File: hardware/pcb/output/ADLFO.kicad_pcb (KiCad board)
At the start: 2 copper layers, 116.6 x 110.5 mm, 118 parts, among them J1 TRIG1, J10 TRIG4, J11 CV4, J12 OUT4, J13 EURORACK 2x5 keyed, J14 OLED SSD1306 128x64, J2 CV1, J3 OUT1, J4 TRIG2, J5 CV2, J6 OUT2, J7 TRIG3, J8 CV3, J9 OUT3, Q1 MMBT3904, Q2 MMBT3904, Q3 MMBT3904, Q4 MMBT3904, SW1 CH 1, SW2 CH 2, SW3 CH 3, SW4 CH 4, U1 Daisy Seed (socketed), U2 MCP4728-E/UN, U3 MCP6004-I/SL, U4 TL074CDR, U5 R-78E5.0-0.5

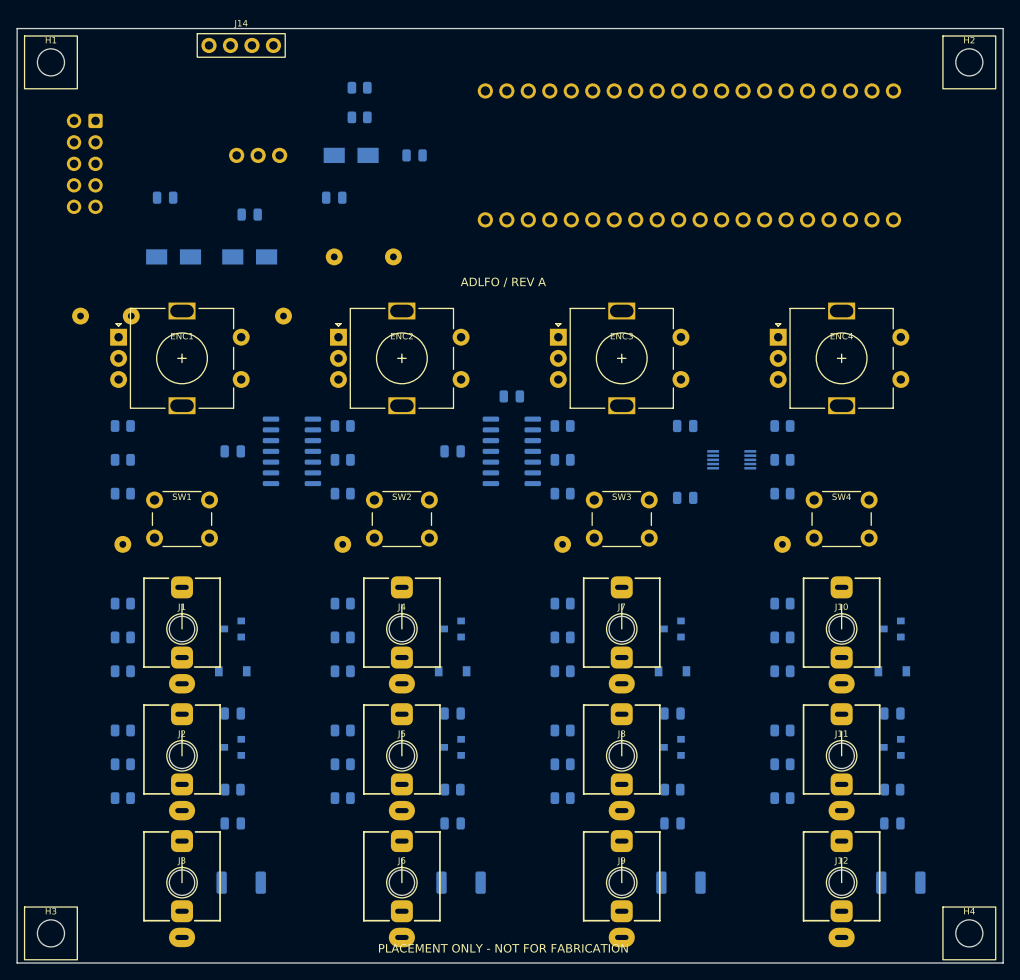
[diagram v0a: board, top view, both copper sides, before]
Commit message: Adapt PCB placement to 20 HP with Adafruit DAC module and Eurorack power provisions
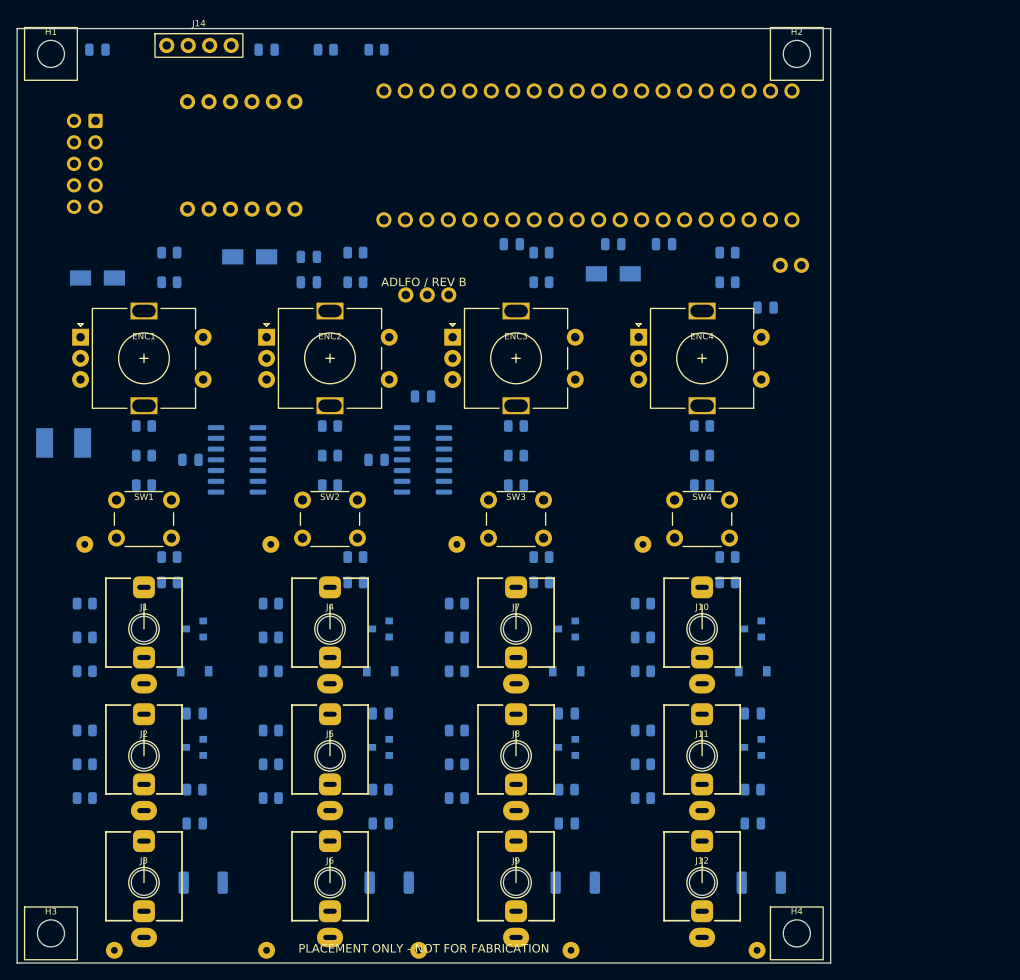
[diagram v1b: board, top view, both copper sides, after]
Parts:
- added C10: 47uF 10V low ESR candidate, ADLFO:radial_cap, B.Cu at (94.0, 37.0)
- added C11: 100nF, ADLFO:c0805, B.Cu at (79.0, 34.5)
- added C12: 100nF, ADLFO:c0805, B.Cu at (91.0, 42.0)
- added F1: PTC 0.5A hold candidate, ADLFO:ptc1812, B.Cu at (8.00, 58.0)
- added RP11: 10k DNP, ADLFO:r0805, B.Cu at (20.5, 35.5)
- added RP12: 10k DNP, ADLFO:r0805, B.Cu at (20.5, 39.0)
- added RP13: 10k DNP, ADLFO:r0805, B.Cu at (20.5, 71.5)
- added RP14: 10k DNP, ADLFO:r0805, B.Cu at (20.5, 74.5)
- added RP21: 10k DNP, ADLFO:r0805, B.Cu at (42.5, 35.5)
- added RP22: 10k DNP, ADLFO:r0805, B.Cu at (42.5, 39.0)
- added RP23: 10k DNP, ADLFO:r0805, B.Cu at (42.5, 71.5)
- added RP24: 10k DNP, ADLFO:r0805, B.Cu at (42.5, 74.5)
- added RP31: 10k DNP, ADLFO:r0805, B.Cu at (64.5, 35.5)
- added RP32: 10k DNP, ADLFO:r0805, B.Cu at (64.5, 39.0)
- added RP33: 10k DNP, ADLFO:r0805, B.Cu at (64.5, 71.5)
- added RP34: 10k DNP, ADLFO:r0805, B.Cu at (64.5, 74.5)
- added RP41: 10k DNP, ADLFO:r0805, B.Cu at (86.5, 35.5)
- added RP42: 10k DNP, ADLFO:r0805, B.Cu at (86.5, 39.0)
- added RP43: 10k DNP, ADLFO:r0805, B.Cu at (86.5, 71.5)
- added RP44: 10k DNP, ADLFO:r0805, B.Cu at (86.5, 74.5)
- R1, R2: value 4.7k -> 4.7k DNP
- U2: value MCP4728-E/UN -> Adafruit MCP4728 STEMMA QT breakout; footprint ADLFO:msop10 -> ADLFO:mcp4728_breakout
- moved TP5 92.6 mm to (90.0, 118.0)
- moved TP4 86.6 mm to (68.0, 118.0)
- moved TP2 76.7 mm to (32.0, 118.0)
- moved TP3 76.7 mm to (50.0, 118.0)
- moved TP1 75.1 mm to (14.0, 118.0)
- moved U2 68.3 mm to (29.0, 24.0)
- moved C6 51.3 mm to (37.0, 39.0)
- moved C5 48.8 mm to (37.0, 36.0)
- moved D3 34.0 mm to (73.0, 38.0)
- moved U5 25.9 mm to (51.0, 40.5)
- moved C4 25.7 mm to (73.0, 34.5)
- moved C3 21.7 mm to (61.0, 34.5)
- moved H2 20.4 mm to (94.7, 12.0)
- moved H4 20.4 mm to (94.7, 116.0)
- moved C2 19.6 mm to (32.0, 11.5)
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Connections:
- D1 pad 2: +12V_IN -> +12V_FUSED
- U2 pad 10: GND -> DAC3
- U2 pad 2: D11 -> GND
- U2 pad 3: D12 -> D11
- U2 pad 4: GND -> D12
- U2 pad 5: (no net) -> GND
- U2 pad 6: DAC1 -> (no net)
- U2 pad 7: DAC2 -> GND
- U2 pad 8: DAC3 -> DAC1
- U2 pad 9: DAC4 -> DAC2
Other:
- board size 116.6 x 110.5 mm -> 96.2 x 110.5 mm
- board text added: "ADLFO / REV B"
- board text removed: "ADLFO / REV A"
